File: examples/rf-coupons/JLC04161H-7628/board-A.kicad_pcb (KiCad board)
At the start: 4 copper layers, 176 x 182 mm, 80 parts, among them X10 TestPoint_PTH, X11 TestPoint_PTH, X12 TestPoint_PTH, X13 TestPoint_PTH, X14 TestPoint_PTH, X15 TestPoint_PTH, X16 TestPoint_PTH, X17 TestPoint_PTH, X18 TestPoint_PTH, X19 TestPoint_PTH, X20 TestPoint_PTH, X21 TestPoint_PTH, X22 TestPoint_PTH, X23 TestPoint_PTH, X24 TestPoint_PTH, X25 TestPoint_PTH, X26 TestPoint_PTH, X27 TestPoint_PTH, X28 TestPoint_PTH, X29 TestPoint_PTH, X3 TestPoint_PTH, X30 TestPoint_PTH, X31 TestPoint_PTH, X32 TestPoint_PTH, X33 TestPoint_PTH, X34 TestPoint_PTH, X35 TestPoint_PTH, X36 TestPoint_PTH, X37 TestPoint_PTH, X38 TestPoint_PTH, X4 TestPoint_PTH, X42 Microsection, X43 Anchor, X46 NetTie_Short, X49 Anchor, X5 TestPoint_PTH, X58 Anchor, X59 Anchor, X6 TestPoint_PTH, X7 TestPoint_PTH, X8 TestPoint_PTH, X9 TestPoint_PTH

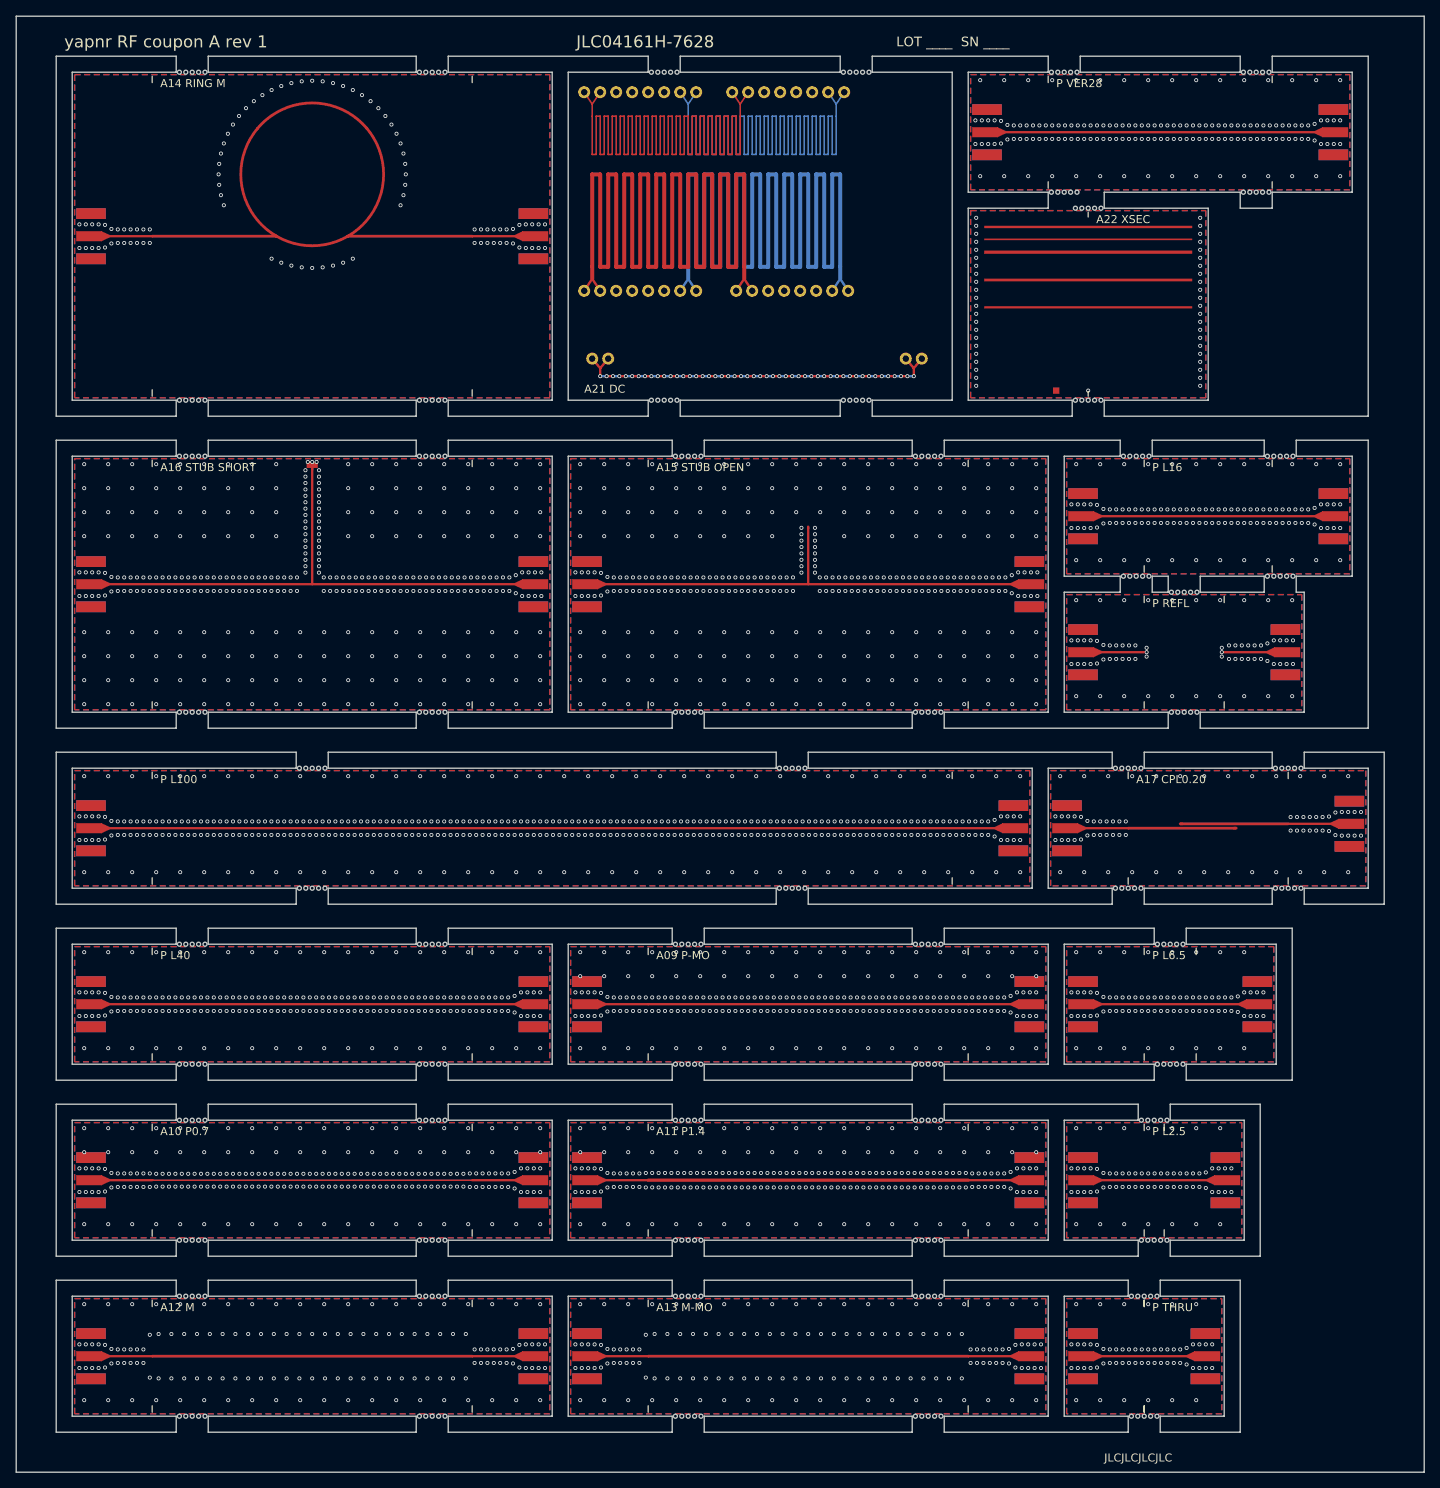
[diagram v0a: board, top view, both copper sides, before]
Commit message: RF coupons: stick ids on every label, 5 mm mouse-bite tabs, fab notes (#32)
Boards (regenerated; KiCad 10.0.6 DRC: 0 violations, 0 unconnected):
- The TRL-set sticks were labelled "P L40" with no stick id. That
  covered the whole TRL set of both boards, including board B's P tie
  set. The session file names need the id (A-03_A05-P-L40_r1.s2p), and
  design 5.5 asks for it. Every label now starts with its id. A label
  too long for a 20 mm thru ends 0.5 mm from the far edge. Labels now
  sit 1.6-2.6 mm from the long edge, below the reference-plane ticks
  (0.5-1.3 mm). The second tick of the 2.5 and 6.5 mm lines used to
  cross the text.
- Mouse-bite tabs widen from 4 mm to 5 mm, with six 0.5 mm bites at
  0.8 mm pitch. JLC's capabilities page (read 2026-10-02) asks for at
  least 5 mm on a tab with mouse bites.

Fab notes:
- They list M (0.348 mm) and say that no width or gap of any test
  structure may be changed.
- The edge clearance moves from "unverified" to checked: JLC asks for
  0.2 mm on routed edges; the zones keep 0.30 mm and DRC checks 0.25 mm.

Other changes:
- JLC06161H-7628 L4-L6 and JLC06161H-2116C L4-L6 are marked verified
  against jlcpcb.com/impedance (read 2026-10-02, and main's
  yapnr/fab/data/stackups). The values are unchanged.
- The expected-file headers no longer repeat the id.
- test_catalog checks that every label carries its id, fits its stick
  and clears the ticks.

Co-Authored-By: Claude Opus 5.5 <noreply@anthropic.com>
Claude-Session: https://claude.ai/code/session_01NY8rMuBH8hTFjkoZyuqNZ7
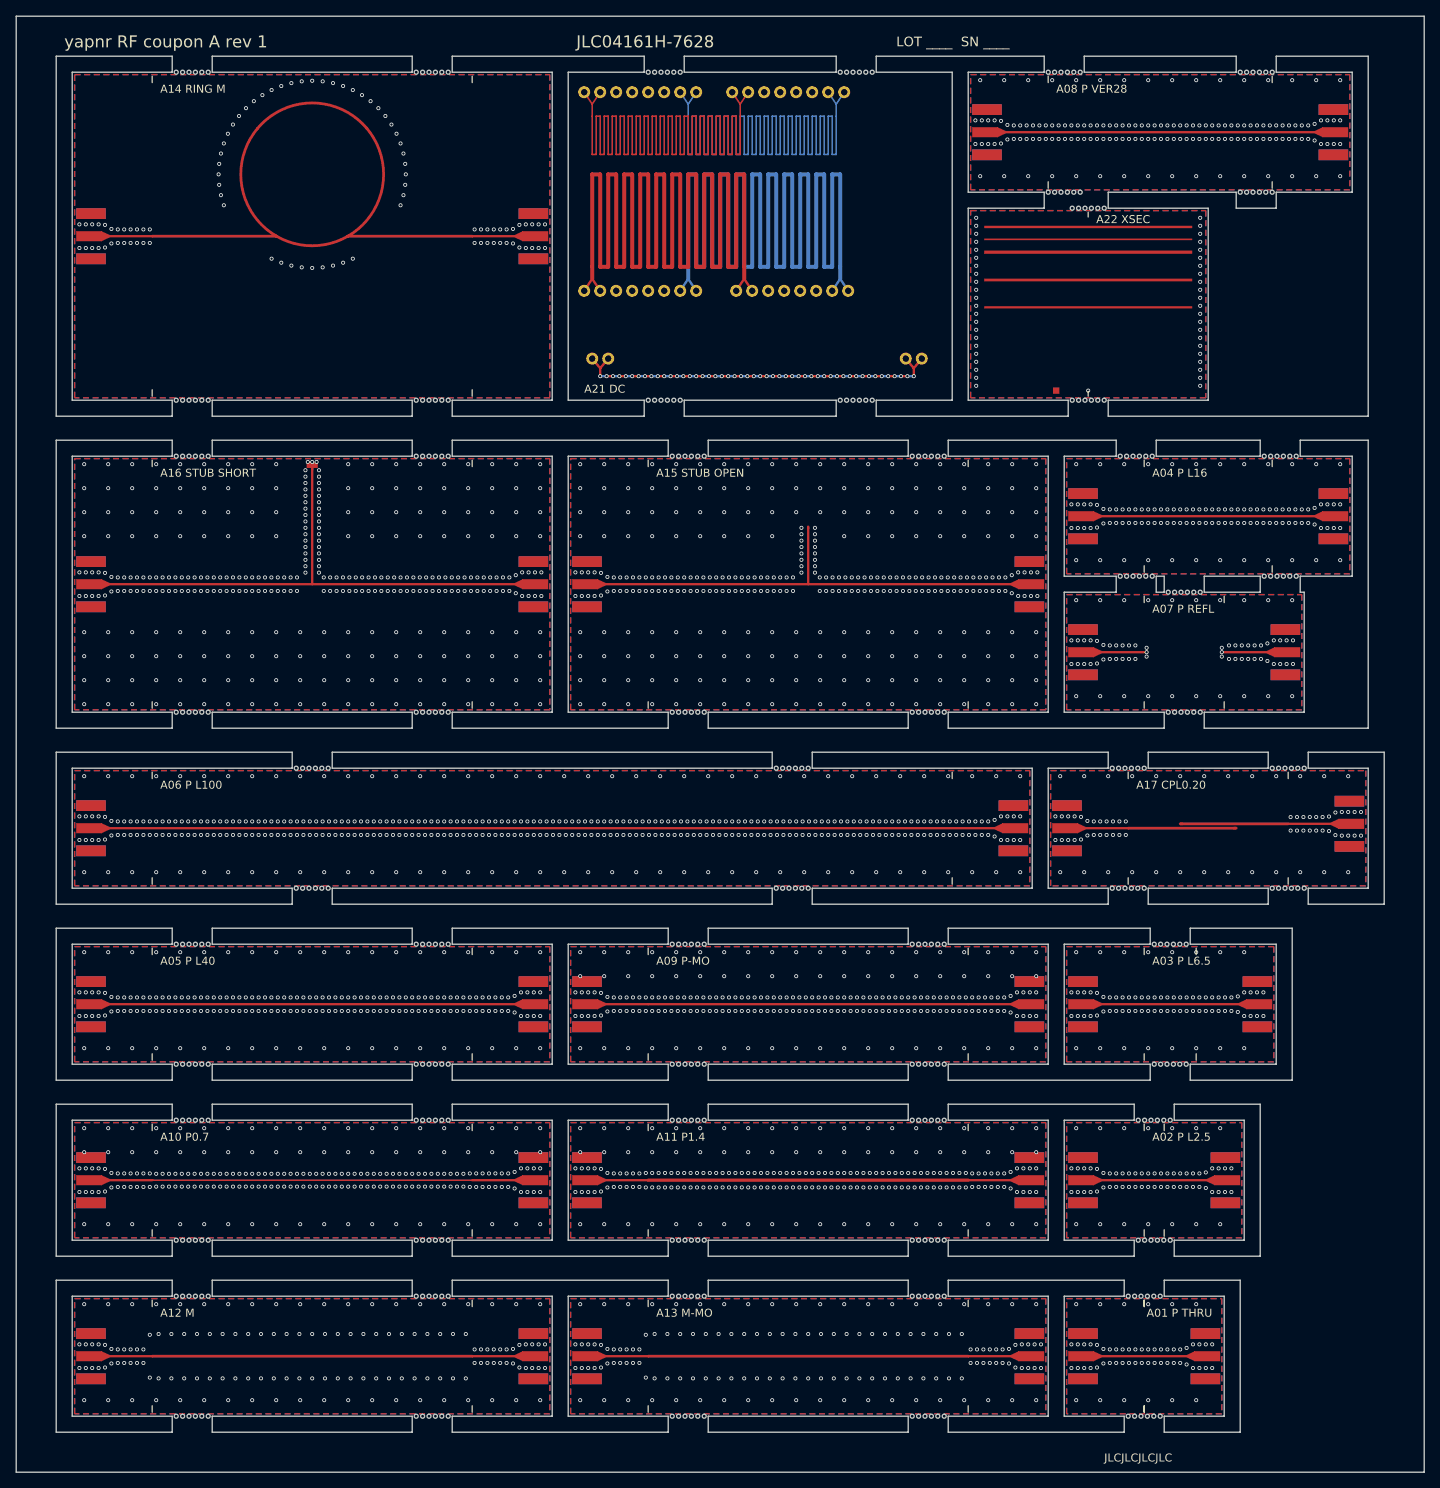
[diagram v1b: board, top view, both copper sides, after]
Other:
- outline, holes or cut-outs redrawn
- board text added: "A01 P THRU"
- board text added: "A02 P L2.5"
- board text added: "A03 P L6.5"
- board text added: "A04 P L16"
- board text added: "A05 P L40"
- board text added: "A06 P L100"
- board text added: "A07 P REFL"
- board text added: "A08 P VER28"
- board text removed: "P L100"
- board text removed: "P L16"
- board text removed: "P L2.5"
- board text removed: "P L40"
- board text removed: "P L6.5"
- board text removed: "P REFL"
- board text removed: "P THRU"
- board text removed: "P VER28"

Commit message: Order 0 part 2: run 0b, D1/D2 designs, predictions and pre-registration bundle, OSH Park fab files (#45)
Order 0 part 2 (the OSH Park 4-layer RF demo): part 1's boards
(`claude/order0`, merged here onto main) plus the setup of the optimizer
demos D1/D2. Draft: the compute stage (D1/D2 runs, predictions, window
fill and labels) will add to it.

## What is in it

- **Part 1** (`claude/order0`, 25 commits): board O (the three uploads
O0-M, O0-W, O0-D), the Cinch 142-0701-851 launch, coupon predictions,
the `docs/rf/order0/` pages. Main already carried the RF coupons as
squashed #35; the merge keeps main's `//yapnr/rf:package` dependency and
both docs index entries.
- **RF stage plans require the native kernel**
(`tools/exp/rf_stage_plan.py`, the PR #30 review's follow-up): every
line sets `YAPNR_RF_THREADS` (re-validations included, which ran on
their run's spec threads) and `YAPNR_RF_REQUIRE_NATIVE=1` unless a job
opts out; jobs take `backend`, `dtype` and `env` (`YAPNR_RF_*`);
`--image-commit REV` refuses, before any upload, a bundle whose native C
sources are not the image's while a job requires the library; the
manifest records both sha256. The diagnostic's `ok` requires the library
when asked. Tests for each.
- **Thickness-equivalent substrates** (`yapnr.rf.coupons.equivalent`,
D-O0-9): 2D quasi-static solves of the real 43 µm strip on the region's
dielectric stack against a zero-thickness sheet (a line conductor;
within 0.06 % of Hammerstad-Jensen), matched to the coupon forward
model's line at 5 GHz (its Djordjevic-Sarkar εr and rough-copper
internal inductance) and to the geometric target; M and W on FR408HR and
EM528. M-eq FR408HR: εr' 3.4417, h' 0.1795 mm, tan δ' 0.0088 (the plan's
closed-form estimate was 3.40 / 0.176).
- **`yapnr.rf.order0`**: D1/D2 specs in four formulations (the plan's V3
baseline; a wider robust set from β = 8; the junction start; a longer
plain epoch with the epoch-best trust reference) and a selection rule
fixed before any run; criteri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
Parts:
- moved MO_A13 20.3 mm to (99.0, 183.8)
- moved MO_A09 20.1 mm to (99.0, 141.7)
- moved MO_A22_PMO 13.5 mm to (140.5, 55.2)
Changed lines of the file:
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@@
 		(fp_rect (start -2.35 -3.75) (end 2.1 3.75) (stroke (width 0.05) (type solid)) (fill no) (layer "F.CrtYd"))
 	)
-	(footprint "MaskOpening" (layer "F.Cu") (at 154 56.3955 0)
+	(footprint "MaskOpening" (layer "F.Cu") (at 140.5 55.25 0)
 		(property "Reference" "MO_A22_PMO" (at 0 0 0) (layer "F.Fab") (effects (font (size 0.8 0.8) (thickness 0.12))))
 		(property "Value" "MaskOpening" (at 0 0 0) (layer "F.Fab") (hide yes) (effects (font (size 0.8 0.8) (thickness 0.12))))
 		(attr smd)
-		(fp_poly (pts (xy -13.5 -1.1455) (xy 13.5 -1.1455) (xy 13.5 1.1455) (xy -13.5 1.1455)) (stroke (width 0) (type solid)) (fill yes) (layer "F.Mask"))
+		(fp_poly (pts (xy 0 0) (xy 27 0) (xy 27 2.291) (xy 0 2.291)) (stroke (width 0) (type solid)) (fill yes) (layer "F.Mask"))
 	)
 	(footprint "Microsection" (layer "F.Cu") (at 154 56 0)
@@
 		(fp_rect (start -2.35 -3.75) (end 2.1 3.75) (stroke (width 0.05) (type solid)) (fill no) (layer "F.CrtYd"))
 	)
-	(footprint "MaskOpening" (layer "F.Cu") (at 119 143.5 0)
+	(footprint "MaskOpening" (layer "F.Cu") (at 99 141.65 0)
 		(property "Reference" "MO_A09" (at 0 0 0) (layer "F.Fab") (effects (font (size 0.8 0.8) (thickness 0.12))))
 		(property "Value" "MaskOpening" (at 0 0 0) (layer "F.Fab") (hide yes) (effects (font (size 0.8 0.8) (thickness 0.12))))
 		(attr smd)
-		(fp_poly (pts (xy -20 -1.8455) (xy 20 -1.8455) (xy 20 1.8455) (xy -20 1.8455)) (stroke (width 0) (type solid)) (fill yes) (layer "F.Mask"))
+		(fp_poly (pts (xy 0 0.0045) (xy 40 0.0045) (xy 40 3.6955) (xy 0 3.6955)) (stroke (width 0) (type solid)) (fill yes) (layer "F.Mask"))
 	)
 	(footprint "SMA_EdgeLaunch_SMA-J-P-H-ST-EM1" (layer "F.Cu") (at 153.1 143.5 180)
@@
 		(fp_rect (start -2.35 -3.75) (end 2.1 3.75) (stroke (width 0.05) (type solid)) (fill no) (layer "F.CrtYd"))
 	)
-	(footprint "MaskOpening" (layer "F.Cu") (at 119 187.5 0)
+	(footprint "MaskOpening" (layer "F.Cu") (at 99 183.83 0)
 		(property "Reference" "MO_A13" (at 0 0 0) (layer "F.Fab") (effects (font (size 0.8 0.8) (thickness 0.12))))
 		(property "Value" "MaskOpening" (at 0 0 0) (layer "F.Fab") (hide yes) (effects (font (size 0.8 0.8) (thickness 0.12))))
 		(attr smd)
-		(fp_poly (pts (xy -20 -3.674) (xy 20 -3.674) (xy 20 3.674) (xy -20 3.674)) (stroke (width 0) (type solid)) (fill yes) (layer "F.Mask"))
+		(fp_poly (pts (xy 0 -0.004) (xy 40 -0.004) (xy 40 7.344) (xy 0 7.344)) (stroke (width 0) (type solid)) (fill yes) (layer "F.Mask"))
 	)
 	(footprint "SMA_EdgeLaunch_SMA-J-P-H-ST-EM1" (layer "F.Cu") (at 153.1 187.5 180)
